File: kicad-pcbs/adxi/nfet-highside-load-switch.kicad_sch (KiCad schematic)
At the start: 7 parts, among them Q19 2N7002, Q20 HY1904C2

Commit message: More bands
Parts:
- renumbered D16 to D12, Q19 to Q11, Q20 to Q12, R48 to R32, R49 to R33, R50 to R34, R51 to R35

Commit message: Updates
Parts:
- renumbered D12 to D16, Q11 to Q19, Q12 to Q20, R32 to R48, R33 to R49, R34 to R50, R35 to R51

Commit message: Pluggable PAs
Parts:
- renumbered D16 to D21, Q19 to Q29, Q20 to Q30, R48 to R68, R49 to R69, R50 to R70, R51 to R71
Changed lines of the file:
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@@
 		(on_board yes)
 		(dnp no)
-		(property "Reference" "Q20"
+		(property "Reference" "Q30"
 			(at 173.99 70.739 0)
 			(effects
@@
 		(on_board yes)
 		(dnp no)
-		(property "Reference" "D16"
+		(property "Reference" "D21"
 			(at 153.035 84.455 90)
 			(effects
@@
 		(on_board yes)
 		(dnp no)
-		(property "Reference" "R48"
+		(property "Reference" "R68"
 			(at 114.935 88.773 90)
 			(effects
@@
 		(on_board yes)
 		(dnp no)
-		(property "Reference" "Q19"
+		(property "Reference" "Q29"
 			(at 130.2766 92.8116 0)
 			(effects
@@
 		(on_board yes)
 		(dnp no)
-		(property "Reference" "R50"
+		(property "Reference" "R70"
 			(at 137.6172 71.8566 0)
 			(effects
@@
 		(on_board yes)
 		(dnp no)
-		(property "Reference" "R49"
+		(property "Reference" "R69"
 			(at 131.6228 71.8566 0)
 			(effects
@@
 		(on_board yes)
 		(dnp no)
-		(property "Reference" "R51"
+		(property "Reference" "R71"
 			(at 141.605 83.693 90)
 			(effects

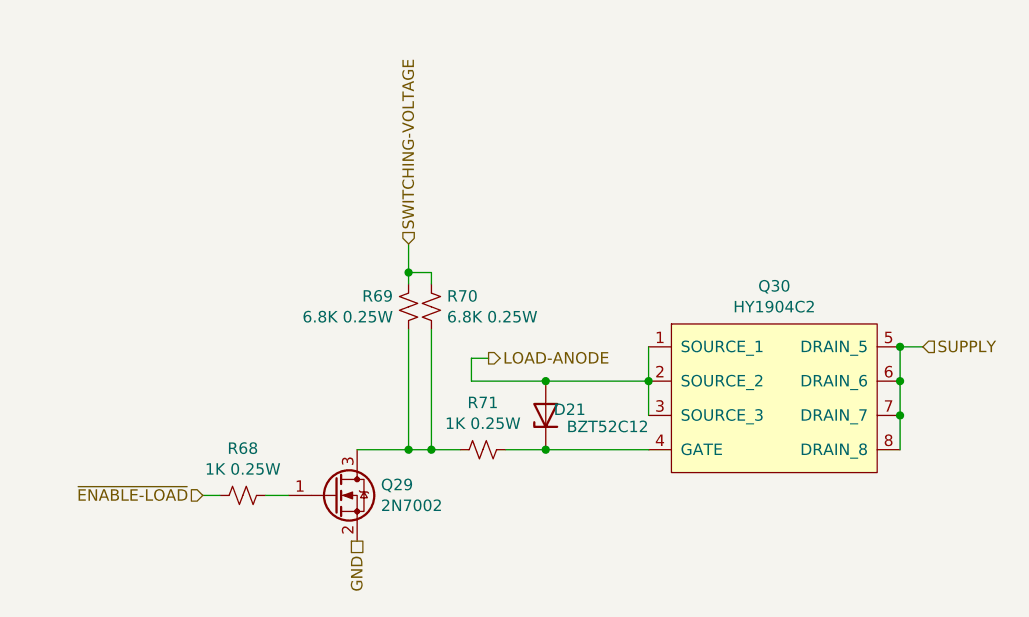
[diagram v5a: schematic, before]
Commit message: Further PA choke work
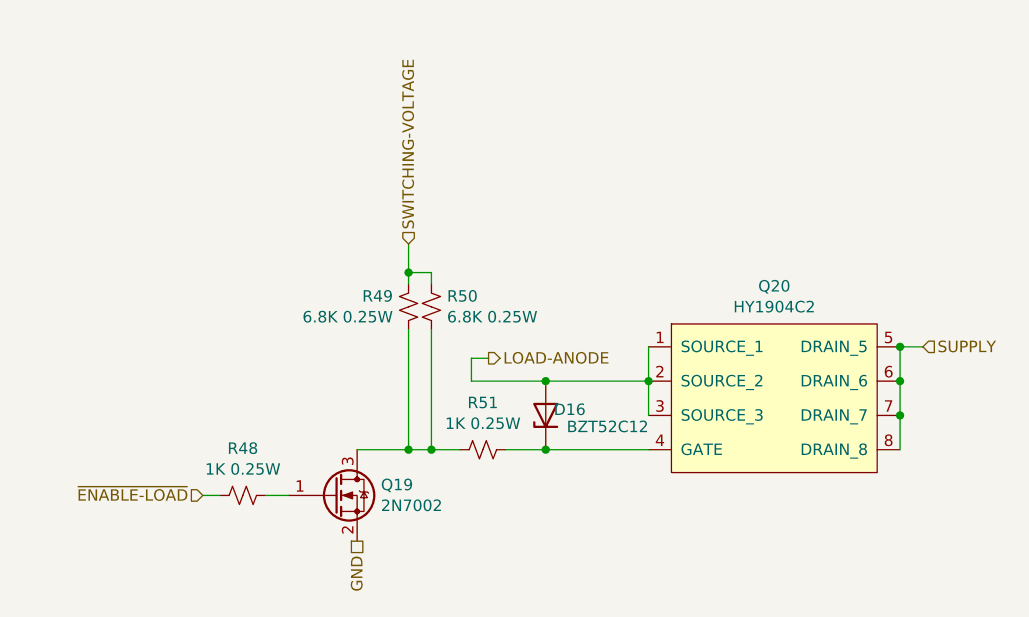
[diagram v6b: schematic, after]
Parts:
- renumbered D21 to D16, Q29 to Q19, Q30 to Q20, R68 to R48, R69 to R49, R70 to R50, R71 to R51
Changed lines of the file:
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@@
 		(on_board yes)
 		(dnp no)
-		(property "Reference" "Q30"
+		(property "Reference" "Q20"
 			(at 173.99 70.739 0)
 			(effects
@@
 		(on_board yes)
 		(dnp no)
-		(property "Reference" "D21"
+		(property "Reference" "D16"
 			(at 153.035 84.455 90)
 			(effects
@@
 		(on_board yes)
 		(dnp no)
-		(property "Reference" "R68"
+		(property "Reference" "R48"
 			(at 114.935 88.773 90)
 			(effects
@@
 		(on_board yes)
 		(dnp no)
-		(property "Reference" "Q29"
+		(property "Reference" "Q19"
 			(at 130.2766 92.8116 0)
 			(effects
@@
 		(on_board yes)
 		(dnp no)
-		(property "Reference" "R70"
+		(property "Reference" "R50"
 			(at 137.6172 71.8566 0)
 			(effects
@@
 		(on_board yes)
 		(dnp no)
-		(property "Reference" "R69"
+		(property "Reference" "R49"
 			(at 131.6228 71.8566 0)
 			(effects
@@
 		(on_board yes)
 		(dnp no)
-		(property "Reference" "R71"
+		(property "Reference" "R51"
 			(at 141.605 83.693 90)
 			(effects
